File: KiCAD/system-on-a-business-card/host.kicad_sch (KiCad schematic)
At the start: 24 parts, among them SW2 SW_Push, U2 ESP32-C3, U3 ZD25WQ32C, Y1 40MHz

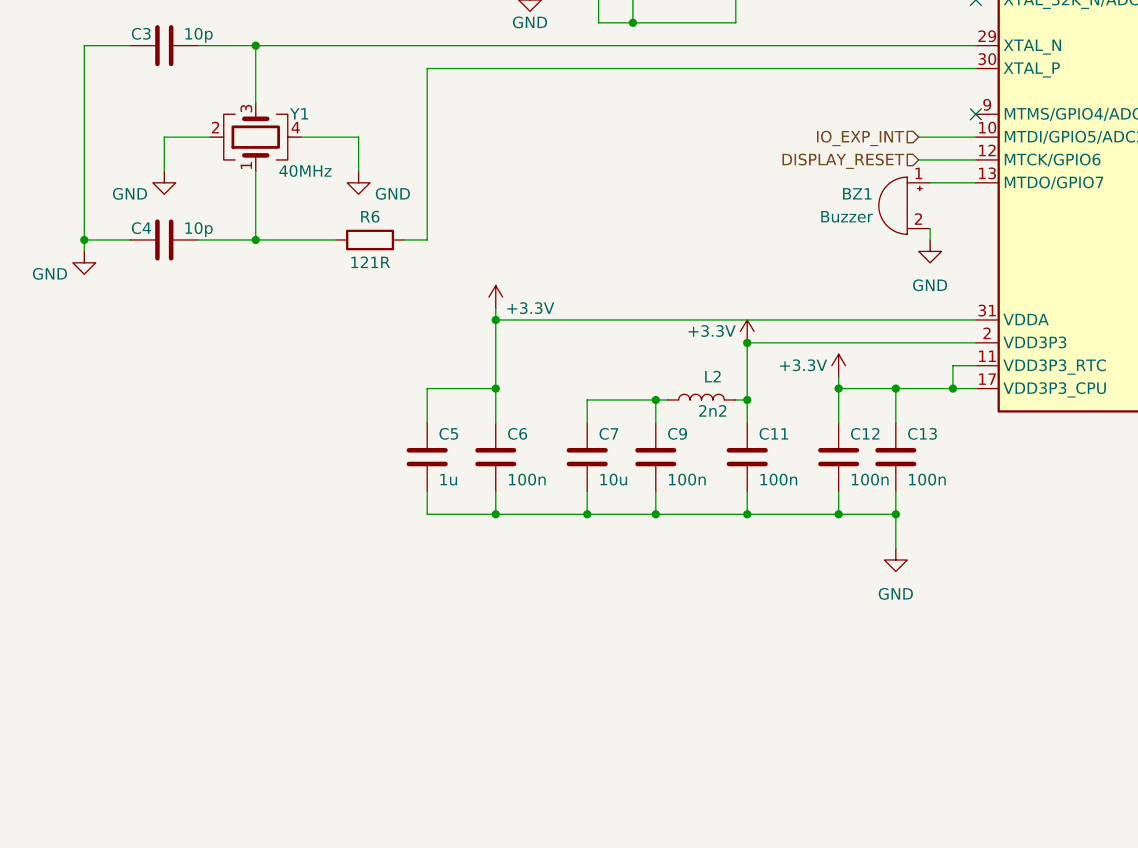
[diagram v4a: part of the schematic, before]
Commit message: #10: updated buzzer circuit
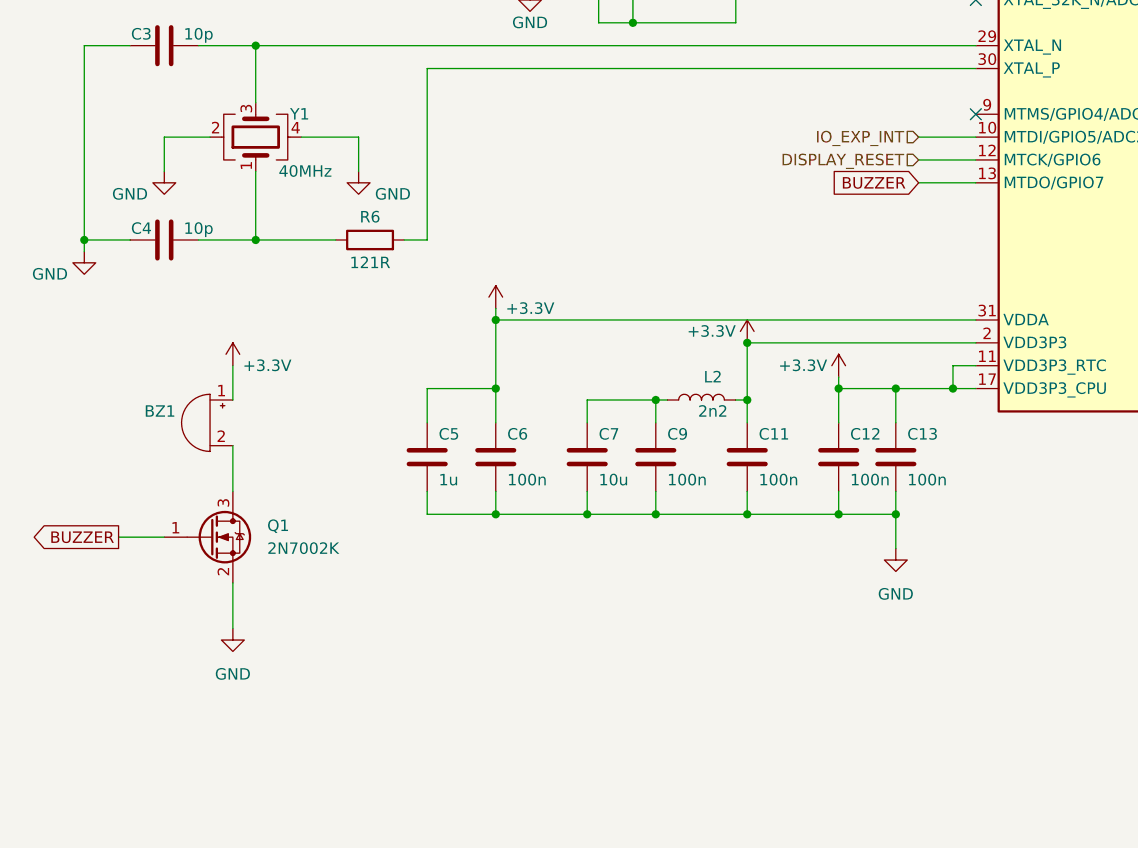
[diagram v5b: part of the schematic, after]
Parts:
- added Q1: 2N7002K, Package_TO_SOT_SMD:SOT-23, symbol Transistor_FET:2N7002K
- BZ1: footprint Buzzer_Beeper:Buzzer_Mallory_AST1109MLTRQ -> Buzzer_Beeper:MagneticBuzzer_CUI_CMT-8504-100-SMT
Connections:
- net +3.3V: now also BZ1.1 (-)
- net GND: now also Q1.2 (S); no longer BZ1.2 (+)
- net BUZZER: now reaches U2.13 (MTDO/GPIO7)
- net BUZZER: now also Q1.1 (G); no longer BZ1.1 (-)
- new net: BZ1.2 (+), Q1.3 (D)
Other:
- moved on the sheet: BZ1
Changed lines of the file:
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@@
     (stroke (width 0) (type default))
   )
-  (wire (pts (xy 121.92 68.58) (xy 121.92 67.31))
+  (wire (pts (xy 44.45 111.76) (xy 44.45 106.68))
     (stroke (width 0) (type default))
   )
@@
     (stroke (width 0) (type default))
   )
+  (wire (pts (xy 31.75 101.6) (xy 36.83 101.6))
+    (stroke (width 0) (type default))
+  )
   (wire (pts (xy 257.81 43.18) (xy 257.81 39.37))
     (stroke (width 0) (type default))
@@
     (stroke (width 0) (type default))
   )
+  (wire (pts (xy 44.45 91.44) (xy 44.45 96.52))
+    (stroke (width 0) (type default))
+  )
   (wire (pts (xy 27.94 68.58) (xy 33.02 68.58))
     (stroke (width 0) (type default))
@@
     (stroke (width 0) (type default))
   )
+  (wire (pts (xy 44.45 82.55) (xy 44.45 86.36))
+    (stroke (width 0) (type default))
+  )
   (wire (pts (xy 83.82 99.06) (xy 91.44 99.06))
     (stroke (width 0) (type default))
@@
     (stroke (width 0) (type default))
   )
-  (wire (pts (xy 121.92 62.23) (xy 127 62.23))
+  (wire (pts (xy 120.65 62.23) (xy 127 62.23))
     (stroke (width 0) (type default))
   )
@@
   (text "Z=50R" (at 81.28 30.48 0)
     (effects (font (size 1.27 1.27)) (justify left bottom))
+  )
+  (global_label "BUZZER" (shape output) (at 31.75 101.6 180) (fields_autoplaced)
+    (effects (font (size 1.27 1.27)) (justify right))
+    (property "Intersheetrefs" "${INTERSHEET_REFS}" (at 21.3263 101.6 0)
+      (effects (font (size 1.27 1.27)) (justify right) hide)
+    )
+  )
+  (global_label "BUZZER" (shape input) (at 120.65 62.23 180) (fields_autoplaced)
+    (effects (font (size 1.27 1.27)) (justify right))
+    (property "Intersheetrefs" "${INTERSHEET_REFS}" (at 110.2263 62.23 0)
+      (effects (font (size 1.27 1.27)) (justify right) hide)
+    )
   )
   (global_label "BOOT" (shape input) (at 222.25 119.38 0) (fields_autoplaced)
@@
     )
   )
+  (symbol (lib_id "Transistor_FET:2N7002K") (at 41.91 101.6 0) (unit 1)
+    (in_bom yes) (on_board yes) (dnp no) (fields_autoplaced)
+    (property "Reference" "Q1" (at 48.26 100.33 0)
+      (effects (font (size 1.27 1.27)) (justify left))
+    )
+    (property "Value" "2N7002K" (at 48.26 102.87 0)
+      (effects (font (size 1.27 1.27)) (justify left))
+    )
+    (property "Footprint" "Package_TO_SOT_SMD:SOT-23" (at 46.99 103.505 0)
+      (effects (font (size 1.27 1.27) italic) (justify left) hide)
+    )
+    (property "Datasheet" "https://www.diodes.com/assets/Datasheets/ds30896.pdf" (at 41.91 101.6 0)
+      (effects (font (size 1.27 1.27)) (justify left) hide)
+    )
+    (pin "1")
+    (pin "2")
+    (pin "3")
+    (instances
+      (project "system-on-a-business-card"
+        (path "/49855302-2ecc-4f42-8bbd-b9c2e284f529/d51daf21-f243-4884-8481-74d26cfa222b"
+          (reference "Q1") (unit 1)
+        )
+      )
+    )
+  )
   (symbol (lib_id "Device:L") (at 96.52 86.36 90) (unit 1)
     (in_bom yes) (on_board yes) (dnp no)
@@
     )
   )
-  (symbol (lib_id "power:GND") (at 121.92 68.58 0) (unit 1)
+  (symbol (lib_id "power:GND") (at 44.45 111.76 0) (unit 1)
     (in_bom yes) (on_board yes) (dnp no) (fields_autoplaced)
-    (property "Reference" "#PWR050" (at 121.92 74.93 0)
-      (effects (font (size 1.27 1.27)) hide)
-    )
-    (property "Value" "GND" (at 121.92 73.66 0)
-      (effects (font (size 1.27 1.27)))
-    )
-    (property "Footprint" "" (at 121.92 68.58 0)
-      (effects (font (size 1.27 1.27)) hide)
-    )
-    (property "Datasheet" "" (at 121.92 68.58 0)
+    (property "Reference" "#PWR050" (at 44.45 118.11 0)
+      (effects (font (size 1.27 1.27)) hide)
+    )
+    (property "Value" "GND" (at 44.45 116.84 0)
+      (effects (font (size 1.27 1.27)))
+    )
+    (property "Footprint" "" (at 44.45 111.76 0)
+      (effects (font (size 1.27 1.27)) hide)
+    )
+    (property "Datasheet" "" (at 44.45 111.76 0)
       (effects (font (size 1.27 1.27)) hide)
     )
@@
     )
   )
-  (symbol (lib_id "Device:Buzzer") (at 119.38 64.77 0) (mirror y) (unit 1)
-    (in_bom yes) (on_board yes) (dnp no)
-    (property "Reference" "BZ1" (at 115.57 63.5 0)
-      (effects (font (size 1.27 1.27)) (justify left))
-    )
-    (property "Value" "Buzzer" (at 115.57 66.04 0)
-      (effects (font (size 1.27 1.27)) (justify left))
-    )
-    (property "Footprint" "Buzzer_Beeper:Buzzer_Mallory_AST1109MLTRQ" (at 120.015 62.23 90)
-      (effects (font (size 1.27 1.27)) hide)
-    )
-    (property "Datasheet" "~" (at 120.015 62.23 90)
+  (symbol (lib_id "Device:Buzzer") (at 41.91 88.9 0) (mirror y) (unit 1)
+    (in_bom yes) (on_board yes) (dnp no)
+    (property "Reference" "BZ1" (at 38.1 87.63 0)
+      (effects (font (size 1.27 1.27)) (justify left))
+    )
+    (property "Value" "Buzzer" (at 38.1 90.17 0)
+      (effects (font (size 1.27 1.27)) (justify left) hide)
+    )
+    (property "Footprint" "Buzzer_Beeper:MagneticBuzzer_CUI_CMT-8504-100-SMT" (at 42.545 86.36 90)
+      (effects (font (size 1.27 1.27)) hide)
+    )
+    (property "Datasheet" "~" (at 42.545 86.36 90)
       (effects (font (size 1.27 1.27)) hide)
     )
@@
         )
       )
+    )
+  )
+  (symbol (lib_id "power:+3.3V") (at 44.45 82.55 0) (unit 1)
+    (in_bom yes) (on_board yes) (dnp no)
+    (property "Reference" "#PWR026" (at 44.45 86.36 0)
+      (effects (font (size 1.27 1.27)) hide)
+    )
+    (property "Value" "+3.3V" (at 48.26 82.55 0)
+      (effects (font (size 1.27 1.27)))
+    )
+    (property "Footprint" "" (at 44.45 82.55 0)
+      (effects (font (size 1.27 1.27)) hide)
+    )
+    (property "Datasheet" "" (at 44.45 82.55 0)
+      (effects (font (size 1.27 1.27)) hide)
+    )
+    (pin "1")
+    (instances
+      (project "system-on-a-business-card"
+        (path "/49855302-2ecc-4f42-8bbd-b9c2e284f529/d51daf21-f243-4884-8481-74d26cfa222b"
+          (reference "#PWR026") (unit 1)
+        )
+      )

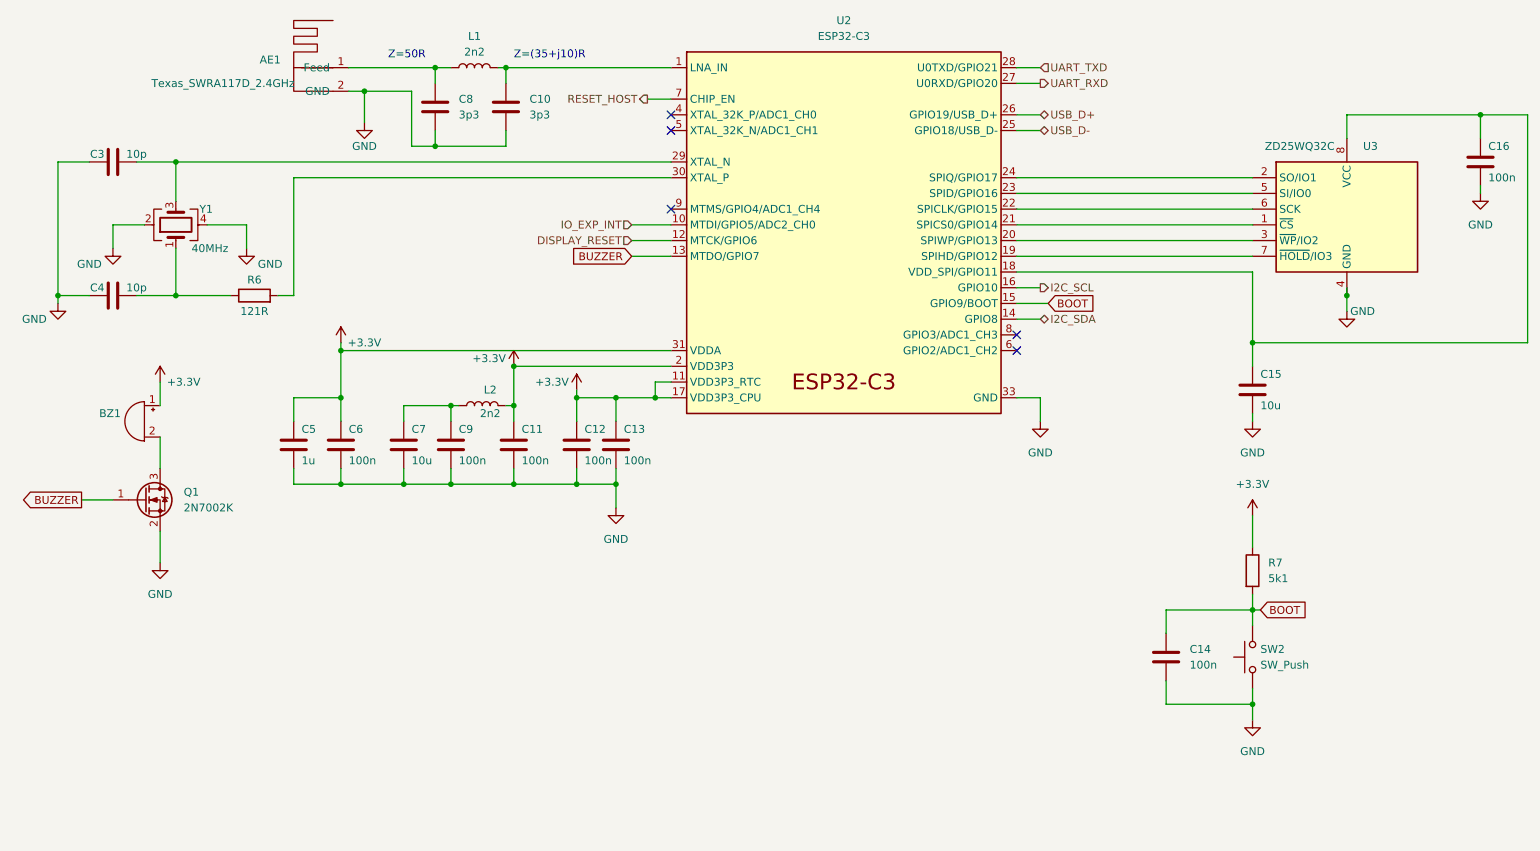
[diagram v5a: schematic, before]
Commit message: #10: continued layouting, added 2nd buzzer
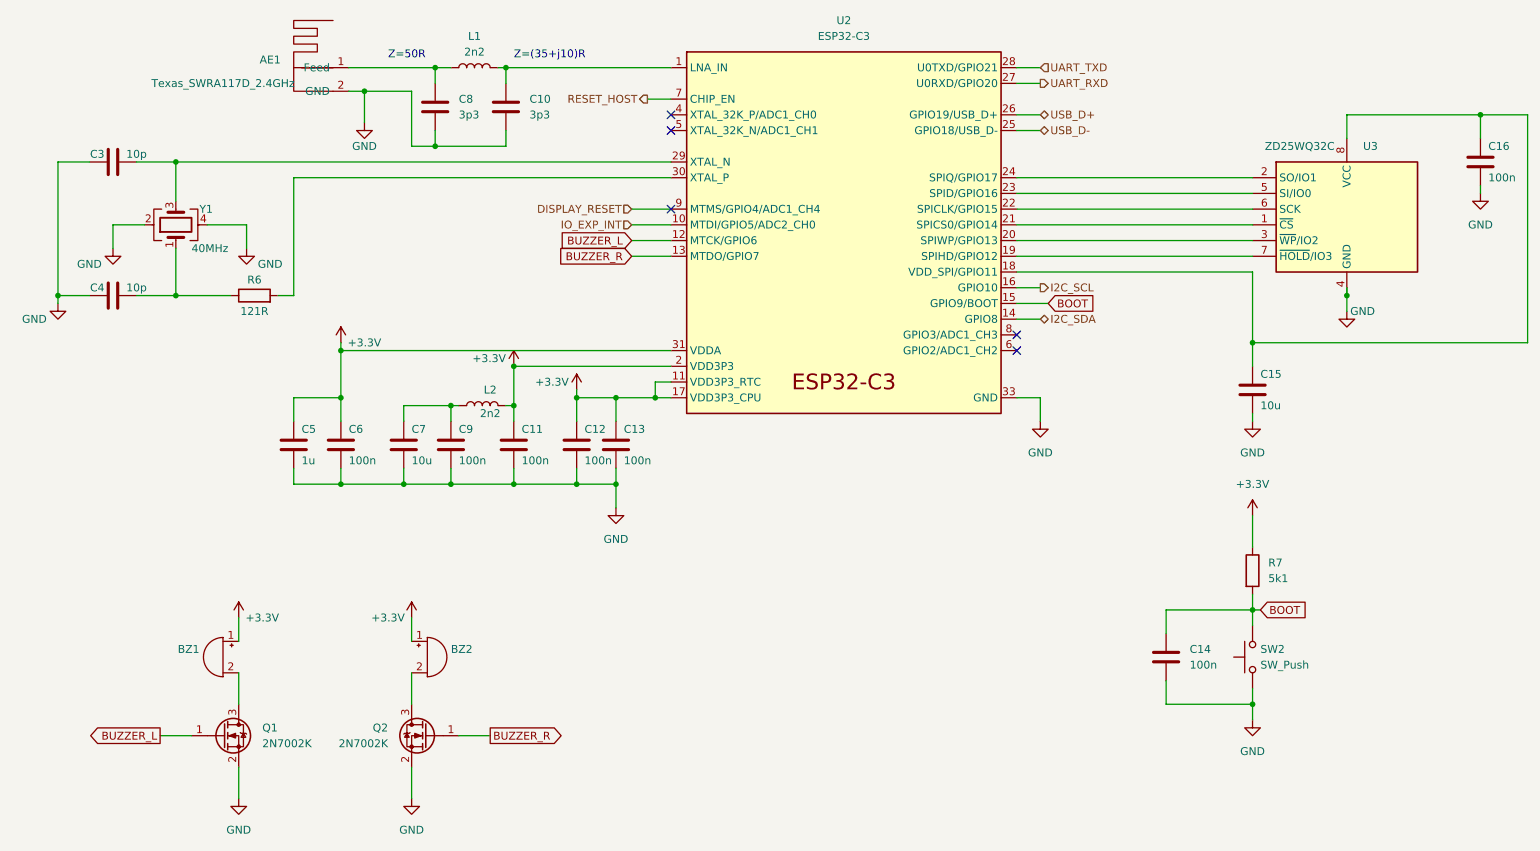
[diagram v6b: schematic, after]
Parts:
- added BZ2: Buzzer, Buzzer_Beeper:MagneticBuzzer_CUI_CMT-8504-100-SMT, symbol Device:Buzzer
- added Q2: 2N7002K, Package_TO_SOT_SMD:SOT-23, symbol Transistor_FET:2N7002K
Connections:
- net +3.3V: now also BZ2.1 (-)
- net DISPLAY_RESET: now also U2.9 (MTMS/GPIO4/ADC1_CH4); no longer U2.12 (MTCK/GPIO6)
- net GND: now also Q2.2 (S)
- net BUZZER renamed BUZZER_L
- net BUZZER_L: now also U2.12 (MTCK/GPIO6); no longer U2.13 (MTDO/GPIO7)
- new net: BZ2.2 (+), Q2.3 (D)
- new net BUZZER_R: Q2.1 (G), U2.13 (MTDO/GPIO7)
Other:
- moved on the sheet: BZ1, Q1

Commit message: #10: started with routing
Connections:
- net BUZZER_L: now also U2.13 (MTDO/GPIO7); no longer U2.12 (MTCK/GPIO6)
- net BUZZER_R: now also U2.12 (MTCK/GPIO6); no longer U2.13 (MTDO/GPIO7)
- no-connect marks 5 -> 4
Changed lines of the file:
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@@
   (no_connect (at 182.88 77.47))
   (no_connect (at 127 39.37))
-  (no_connect (at 127 54.61))
   (no_connect (at 182.88 74.93))
   (no_connect (at 127 41.91))
@@
     )
   )
-  (global_label "BUZZER_R" (shape input) (at 120.65 62.23 180) (fields_autoplaced)
+  (global_label "BUZZER_R" (shape input) (at 120.65 59.69 180) (fields_autoplaced)
     (effects (font (size 1.27 1.27)) (justify right))
-    (property "Intersheetrefs" "${INTERSHEET_REFS}" (at 107.9887 62.23 0)
+    (property "Intersheetrefs" "${INTERSHEET_REFS}" (at 107.9887 59.69 0)
       (effects (font (size 1.27 1.27)) (justify right) hide)
     )
@@
     )
   )
-  (global_label "BUZZER_L" (shape input) (at 120.65 59.69 180) (fields_autoplaced)
+  (global_label "BUZZER_L" (shape input) (at 120.65 62.23 180) (fields_autoplaced)
     (effects (font (size 1.27 1.27)) (justify right))
-    (property "Intersheetrefs" "${INTERSHEET_REFS}" (at 108.2306 59.69 0)
+    (property "Intersheetrefs" "${INTERSHEET_REFS}" (at 108.2306 62.23 0)
       (effects (font (size 1.27 1.27)) (justify right) hide)
     )
